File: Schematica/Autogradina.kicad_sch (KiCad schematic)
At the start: 39 parts, among them IC1 NodeMCU, J1 Priza Pompa, K1 CONTACTOR, P1 Conector putere, P2 Conector periferice 220V, Q1 BC547, Q2 BC547, Q3 BC547, Q4 IRLZ44N, Q5 IRLZ44N, Q6 IRLZ44N, Q7 IRLZ44N, Q8 IRLZ44N

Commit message: Schematic updates; Created board
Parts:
- removed IC1: NodeMCU, symbol Custom:NodeMCU
- removed J1: Priza Pompa, symbol Connector:Conn_WallSocket_Earth
- removed K1: CONTACTOR, Relay_THT:Relay_StandexMeder_DIP_LowProfile, symbol Relay:DIPxx-1Axx-11x
- removed P1: Conector putere, symbol Connector:Conn_01x03_Female
- removed P2: Conector periferice 220V, symbol Connector:Conn_01x06_Female
- removed V1: Conector valve, symbol Connector:Conn_01x10_Female
- added C1: 22uF, Capacitor_THT:CP_Radial_D6.3mm_P2.50mm, symbol Device:C
- added C2: 1uF, Capacitor_THT:CP_Radial_D6.3mm_P2.50mm, symbol Device:C
- added J1: Power_Connector, Custom:Connector_RND_205-00113_3Pins_3.5mm, symbol Connector:Conn_01x03_Socket
- added J2: AC_Connector, Custom:Connector_RND_205-00113_3Pins_3.5mm, symbol Connector:Conn_01x03_Socket
- added J3: UART_Connector, Connector_PinSocket_2.54mm:PinSocket_1x04_P2.54mm_Vertical, symbol Connector:Conn_01x04_Socket
- added J4: USB_B_Micro, Connector_USB:USB_Micro-B_Wuerth_629105150521, symbol Connector:USB_B_Micro
- added J5: Boot_Jumper, Connector_PinHeader_2.54mm:PinHeader_1x02_P2.54mm_Vertical, symbol Connector:Conn_01x02_Pin
- added J6: Ports_Connector, Custom:Connector_Wire-To-Board_10Pins_2.54mm, symbol Connector:Conn_01x10_Socket
- added J7, J8, J9: Conn_01x02_Socket, Custom:Connector_RND_205-00113_2Pins_3.5mm, symbol Connector:Conn_01x02_Socket
- added R1: 180k, Resistor_THT:R_Axial_DIN0207_L6.3mm_D2.5mm_P10.16mm_Horizontal, symbol Device:R
- added R2, R3: 10k, Resistor_THT:R_Axial_DIN0207_L6.3mm_D2.5mm_P10.16mm_Horizontal, symbol Device:R
- added SW1: Reset_Btn, Button_Switch_THT:SW_PUSH_6mm, symbol Switch:SW_Push
- added U1: 4N25, Package_DIP:DIP-6_W7.62mm, symbol Isolator:4N25
- added U2: ESP32-S3-WROOM-1, Expressif:ESP32-S3-WROOM-1U, symbol Expressif:ESP32-S3-WROOM-1
- D1, D2, D3, D4, D5, D6, D7, D8: footprint (none) -> Diode:1N4007
- R10: renamed from R4; footprint (none) -> Resistor_THT:R_Axial_DIN0207_L6.3mm_D2.5mm_P10.16mm_Horizontal
- R11: renamed from R5; footprint (none) -> Resistor_THT:R_Axial_DIN0207_L6.3mm_D2.5mm_P10.16mm_Horizontal
- R12: renamed from R6; footprint (none) -> Resistor_THT:R_Axial_DIN0207_L6.3mm_D2.5mm_P10.16mm_Horizontal
- R13: renamed from R7; footprint (none) -> Resistor_THT:R_Axial_DIN0207_L6.3mm_D2.5mm_P10.16mm_Horizontal
- R14: renamed from R8; footprint (none) -> Resistor_THT:R_Axial_DIN0207_L6.3mm_D2.5mm_P10.16mm_Horizontal
- R15: renamed from R9; footprint (none) -> Resistor_THT:R_Axial_DIN0207_L6.3mm_D2.5mm_P10.16mm_Horizontal
- R16: renamed from R10; footprint (none) -> Resistor_THT:R_Axial_DIN0207_L6.3mm_D2.5mm_P10.16mm_Horizontal
- R4: renamed from R1; footprint (none) -> Resistor_THT:R_Axial_DIN0207_L6.3mm_D2.5mm_P10.16mm_Horizontal
- R5: renamed from R2; footprint (none) -> Resistor_THT:R_Axial_DIN0207_L6.3mm_D2.5mm_P10.16mm_Horizontal
- R6: renamed from R13; footprint (none) -> Resistor_THT:R_Axial_DIN0207_L6.3mm_D2.5mm_P10.16mm_Horizontal
- R7: renamed from R12; footprint (none) -> Resistor_THT:R_Axial_DIN0207_L6.3mm_D2.5mm_P10.16mm_Horizontal
- R8: renamed from R11; footprint (none) -> Resistor_THT:R_Axial_DIN0207_L6.3mm_D2.5mm_P10.16mm_Horizontal
- R9: renamed from R3; footprint (none) -> Resistor_THT:R_Axial_DIN0207_L6.3mm_D2.5mm_P10.16mm_Horizontal
- RTC1: footprint (none) -> Custom:RTC-Module
- renumbered Q4 to Q1, Q5 to Q2, Q6 to Q3, Q7 to Q4, Q8 to Q5, Q1 to Q6, Q2 to Q7, Q3 to Q8
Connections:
- net CONTROL_AC_1 is gone; now on net AC_L: RL1.1, RL1.14
- net CONTROL_AC_2 is gone; now on net AC_L: RL2.1, RL2.14
- net 12V: now also J1.1 (Pin_1), J6.10 (Pin_10), J6.2 (Pin_2), J6.4 (Pin_4), J6.6 (Pin_6), J6.8 (Pin_8)
- net GND: now also C1.2, C2.1, J1.3 (Pin_3), J3.1 (Pin_1), J4.5 (GND), J4.6 (Shield), J5.1 (Pin_1), SW1.1, U1.4, U2.1 (GND), U2.15 (GPIO3/TOUCH3/ADC1_CH2), U2.40 (GND), U2.41 (GND)
- net RTC_CLOCK: now also U2.28 (SPIIO6/GPIO35/FSPID/SUBSPID)
- net RTC_DATA: now also U2.29 (SPIIO7/GPIO36/FSPICLK/SUBSPICLK)
- net at Q1.1 (G), R12.2: now also R11.2; no longer R4.2
- net at D1.2 (A), Q1.2 (D): now also J6.9 (Pin_9)
- net at Q2.1 (G), R13.2: now also R10.2; no longer R5.2
- net at D2.2 (A), Q2.2 (D): now also J6.7 (Pin_7)
- net at D3.2 (A), Q3.2 (D): now also J6.5 (Pin_5)
- net at Q4.1 (G), R15.2: now also R5.2; no longer R10.2
- net at D4.2 (A), Q4.2 (D): now also J6.3 (Pin_3)
- net at Q5.1 (G), R16.2: now also R4.2; no longer R11.2
- net at D5.2 (A), Q5.2 (D): now also J6.1 (Pin_1)
- net RELAY2_CONTROL: now reaches R7.2
- net RELAY2_CONTROL: now also U2.17 (GPIO9/TOUCH9/ADC1_CH8/FSPIHD/SUBSPIHD)
- net RELAY1_CONTROL: now reaches R8.2
- net RELAY1_CONTROL: now also U2.12 (GPIO8/TOUCH8/ADC1_CH7/SUBSPICS1)
- net Mosfet_Port2: now reaches R13.1
- net Mosfet_Port2: now also U2.21 (GPIO13/TOUCH13/ADC2_CH2/FSPIQ/FSPIIO7/SUBSPIQ)
- net Mosfet_Port1: now reaches R12.1
- net Mosfet_Port1: now also U2.20 (GPIO12/TOUCH12/ADC2_CH1/FSPICLK/FSPIIO6/SUBSPICLK)
- net RELAY3_CONTROL: now reaches R6.2
- net RELAY3_CONTROL: now also U2.18 (GPIO10/TOUCH10/ADC1_CH9/FSPICS0/FSPIIO4/SUBSPICS0)
- net Mosfet_Port3: now reaches R14.1
- net Mosfet_Port3: now also U2.22 (GPIO14/TOUCH14/ADC2_CH3/FSPIWP/FSPIDQS/SUBSPIWP)
- net Mosfet_Port5: now reaches R16.1
- net Mosfet_Port5: now also U2.11 (GPIO18/U1RXD/ADC2_CH7/CLK_OUT3)
- net Mosfet_Port4: now reaches R15.1
- net Mosfet_Port4: now also U2.10 (GPIO17/U1TXD/ADC2_CH6)
- net AC_L: now reaches RL3.1, RL3.14
- net AC_L: now also J2.2 (Pin_2)
- net 5V renamed 3.3V
- net 3.3V: now also C1.1, J1.2 (Pin_2), J3.4 (Pin_4), R2.1, R3.1, U2.2 (3V3)
- net RELEU2_CONTROL: no longer names the net of Q7.2 (B), R7.1
- net RELEU3_CONTROL: no longer names the net of Q8.2 (B), R6.1
- removed net SURSA_AC_NUL: RL1.7, RL1.8, RL2.7, RL2.8, RL3.7, RL3.8
- net TIMER_CONTROL: no longer names the net of Q6.2 (B), R8.1
- new net: J7.1 (Pin_1), RL1.7, RL1.8
- new net: J8.1 (Pin_1), RL2.7, RL2.8
- new net: J9.1 (Pin_1), RL3.7, RL3.8
- new net: J3.2 (Pin_2), U2.37 (U0TXD/GPIO43/CLK_OUT1)
- new net: J3.3 (Pin_3), U2.36 (U0RXD/GPIO44/CLK_OUT2)
- new net: R1.1, U1.1
- new net: J5.2 (Pin_2), U2.27 (GPIO0/BOOT)
- new net: C2.2, R2.2, SW1.2, U2.3 (EN)
- new net: J4.2 (D-), U2.13 (GPIO19/U1RTS/ADC2_CH8/CLK_OUT2/USB_D-)
- new net: J4.3 (D+), U2.14 (GPIO20/U1CTS/ADC2_CH9/CLK_OUT1/USB_D+)
- new net AC_G: J2.1 (Pin_1), U1.2
- new net AC_N: J2.3 (Pin_3), J7.2 (Pin_2), J8.2 (Pin_2), J9.2 (Pin_2), R1.2
- new net N_To_Ground_Probe: R3.2, U1.5, U2.39 (GPIO1/TOUCH1/ADC1_CH0)
- no-connect marks 0 -> 6
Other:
- note added: "AC prong inversion detection. Do not allow operation if the AC is inversed as the relays will expose the live wire in this case."
- moved on the sheet: D1, D2, D3, D4, D5, Q1, Q2, Q3, Q4, Q5, Q6, Q7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

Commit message: Updated schematic, board; Almost finished board
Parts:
- removed RL1, RL2, RL3: DIPxx-1Axx-11x, Relay_THT:Relay_StandexMeder_DIP_LowProfile, symbol Relay:DIPxx-1Axx-11x
- added K1, K2, K3: G5LE-1, Relay_THT:Relay_SPDT_Omron-G5LE-1, symbol Relay:G5LE-1
- C2: footprint Capacitor_THT:CP_Radial_D6.3mm_P2.50mm -> Capacitor_THT:CP_Radial_D4.0mm_P2.00mm
- R6, R7, R8: value 10k -> 5k
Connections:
- net 12V: now also K1.2, K2.2, K3.2
- net AC_L: now also K1.1, K2.1, K3.1
- net at D6.2 (A), Q6.1 (C): now also K1.5
- net at D7.2 (A), Q7.1 (C): now also K2.5
- net at D8.2 (A), Q8.1 (C): now also K3.5
- net at J7.1 (Pin_1): now also K1.3
- net at J8.1 (Pin_1): now also K2.3
- net at J9.1 (Pin_1): now also K3.3
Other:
- note added: "Cut the charging circuit because its very bad either way: - for a rechargable battery it leads to overvoltage - else it must be used"
- moved on the sheet: J1, J2, J7, J8, J9, RTC1, U1

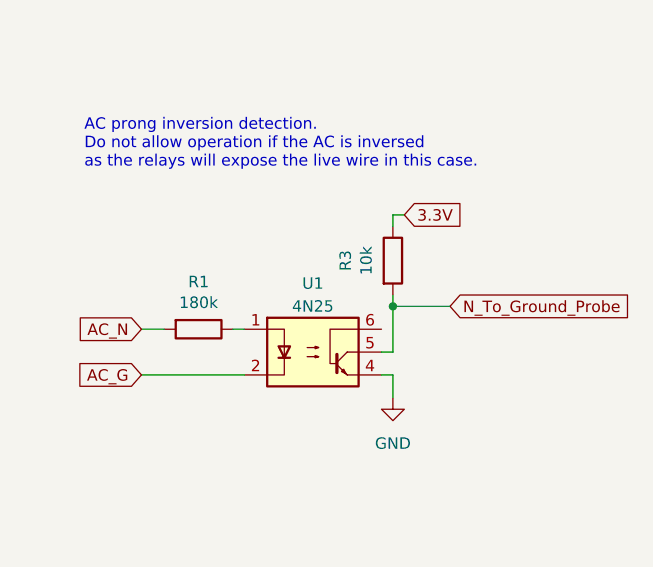
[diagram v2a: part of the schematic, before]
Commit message: Routing changes
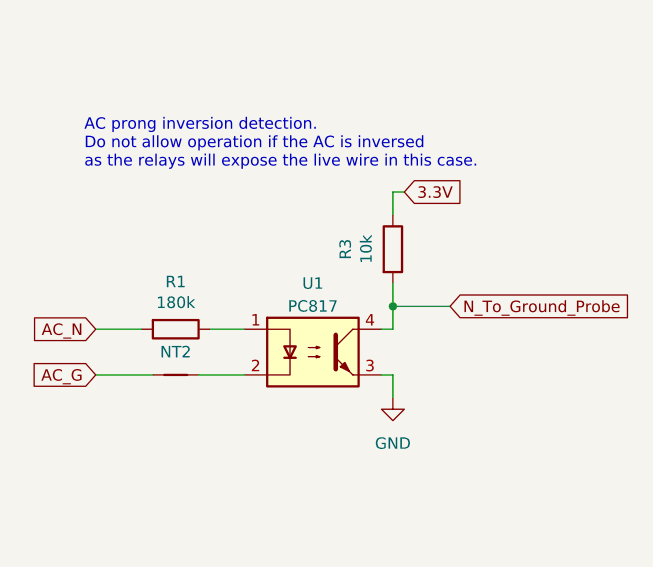
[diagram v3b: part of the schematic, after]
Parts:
- removed U1: 4N25, Package_DIP:DIP-6_W7.62mm, symbol Isolator:4N25
- added NT2: NetTie_2, NetTie:NetTie-2_SMD_Pad0.5mm, symbol Device:NetTie_2
- added U1: PC817, Package_DIP:DIP-4_W7.62mm, symbol Isolator:PC817
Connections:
- net AC_G: now also NT2.1
- net GND: now also U1.3
- net N_To_Ground_Probe: now also U1.4
- net at R1.1: now also U1.1
- new net: NT2.2, U1.2
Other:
- moved on the sheet: R1, R3

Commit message: Repaired too small tracks
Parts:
- removed NT2: NetTie_2, NetTie:NetTie-2_SMD_Pad0.5mm, symbol Device:NetTie_2
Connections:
- net AC_G: now also U1.2
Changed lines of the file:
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@@
-    (stroke (width 0) (type default))
-  )
-  (wire (pts (xy 33.02 200.66) (xy 39.37 200.66))
     (stroke (width 0) (type default))
   )
@@
     (stroke (width 0) (type default))
   )
-  (wire (pts (xy 44.45 200.66) (xy 49.53 200.66))
+  (wire (pts (xy 33.02 200.66) (xy 49.53 200.66))
     (stroke (width 0) (type default))
   )
@@
         )
       )
-    )
-  )
-  (symbol (lib_id "Device:NetTie_2") (at 41.91 200.66 0) (unit 1)
-    (in_bom no) (on_board yes) (dnp no)
-    (property "Reference" "NT2" (at 41.91 198.12 0)
-      (effects (font (size 1.27 1.27)))
-    )
-    (property "Value" "NetTie_2" (at 41.91 199.39 0)
-      (effects (font (size 1.27 1.27)) hide)
-    )
-    (property "Footprint" "NetTie:NetTie-2_SMD_Pad0.5mm" (at 41.91 200.66 0)
-      (effects (font (size 1.27 1.27)) hide)
-    )
-    (property "Datasheet" "~" (at 41.91 200.66 0)
-      (effects (font (size 1.27 1.27)) hide)
-    )
-    (pin "1")
-    (pin "2")
-    (instances
-      (project "Autogradina"
-        (path "/d51b26fb-d168-4a7a-965a-6a8ab4c74219"
-          (reference "NT2") (unit 1)
-        )
-      )
